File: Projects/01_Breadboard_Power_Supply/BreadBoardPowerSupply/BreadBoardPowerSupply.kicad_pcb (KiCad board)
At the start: 2 copper layers, 30.1 x 52.1 mm, 15 parts, among them J1 Barrel_Jack_Switch, J2 Conn_02x02_Odd_Even, J3 Conn_02x02_Odd_Even, SW1 SW_DPDT_x2, U1 LM7805_TO220

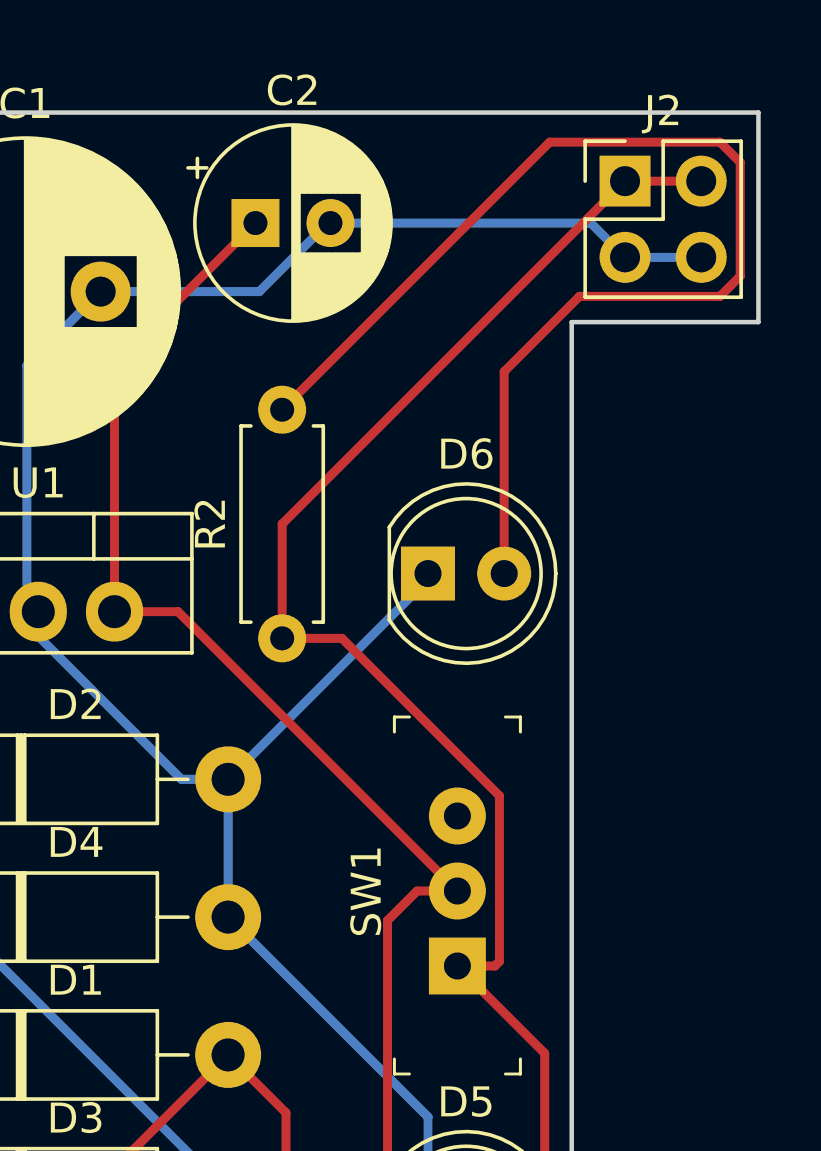
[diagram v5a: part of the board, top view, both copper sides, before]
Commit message: Rotate R2 to shorten wire length of F.Cu and finish routing
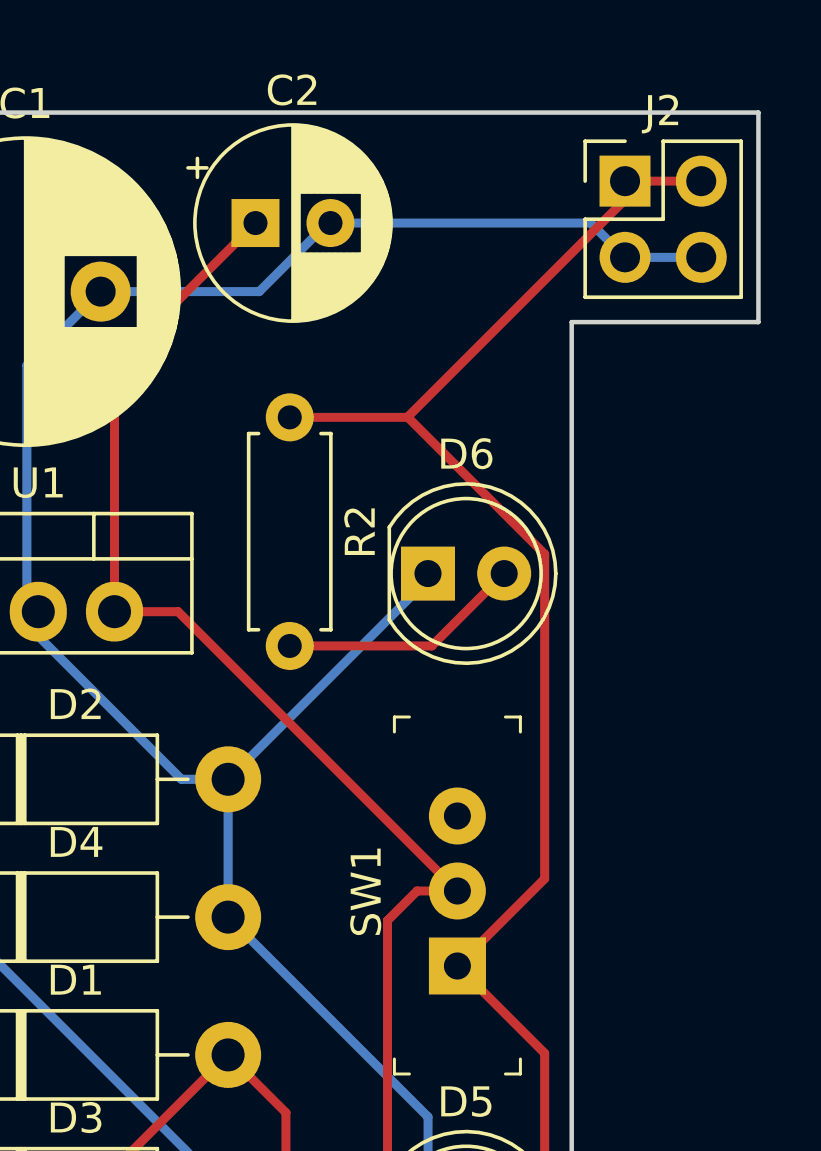
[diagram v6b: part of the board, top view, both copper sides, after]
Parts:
- moved R2 7.37 mm to (137.8, 82.7), turned to 270 degrees
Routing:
- net Net-(D6-Pad2): track 39.0 -> 8.15 mm
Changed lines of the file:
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@@
     (thickness 1.6)
     (drawings 8)
-    (tracks 74)
+    (tracks 68)
     (zones 0)
     (modules 15)
@@
     (add_net /Vout2)
     (add_net "Net-(D3-Pad2)")
+  )
+  (module Resistor_THT:R_Axial_DIN0207_L6.3mm_D2.5mm_P7.62mm_Horizontal (layer F.Cu)
+    (at 137.795 82.677 270)
+    (descr "Resistor, Axial_DIN0207 series, Axial, Horizontal, pin pitch=7.62mm, 0.25W = 1/4W, length*diameter=6.3*2.5mm^2, http://cdn-reichelt.de/documents/datenblatt/B400/1_4W%23YAG.pdf")
+    (tags "Resistor Axial_DIN0207 series Axial Horizontal pin pitch 7.62mm 0.25W = 1/4W length 6.3mm diameter 2.5mm")
+    (fp_text reference R2 (at 3.81 -2.37 90) (layer F.SilkS)
+      (effects (font (size 1 1) (thickness 0.15)))
+    )
+    (fp_text value "560 Ω" (at 3.81 2.37 90) (layer F.Fab)
+      (effects (font (size 1 1) (thickness 0.15)))
+    )
+    (fp_line (start 8.67 -1.5) (end -1.05 -1.5) (layer F.CrtYd) (width 0.05))
+    (fp_line (start 8.67 1.5) (end 8.67 -1.5) (layer F.CrtYd) (width 0.05))
+    (fp_line (start -1.05 1.5) (end 8.67 1.5) (layer F.CrtYd) (width 0.05))
+    (fp_line (start -1.05 -1.5) (end -1.05 1.5) (layer F.CrtYd) (width 0.05))
+    (fp_line (start 7.08 1.37) (end 7.08 1.04) (layer F.SilkS) (width 0.12))
+    (fp_line (start 0.54 1.37) (end 7.08 1.37) (layer F.SilkS) (width 0.12))
+    (fp_line (start 0.54 1.04) (end 0.54 1.37) (layer F.SilkS) (width 0.12))
+    (fp_line (start 7.08 -1.37) (end 7.08 -1.04) (layer F.SilkS) (width 0.12))
+    (fp_line (start 0.54 -1.37) (end 7.08 -1.37) (layer F.SilkS) (width 0.12))
+    (fp_line (start 0.54 -1.04) (end 0.54 -1.37) (layer F.SilkS) (width 0.12))
+    (fp_line (start 7.62 0) (end 6.96 0) (layer F.Fab) (width 0.1))
+    (fp_line (start 0 0) (end 0.66 0) (layer F.Fab) (width 0.1))
+    (fp_line (start 6.96 -1.25) (end 0.66 -1.25) (layer F.Fab) (width 0.1))
+    (fp_line (start 6.96 1.25) (end 6.96 -1.25) (layer F.Fab) (width 0.1))
+    (fp_line (start 0.66 1.25) (end 6.96 1.25) (layer F.Fab) (width 0.1))
+    (fp_line (start 0.66 -1.25) (end 0.66 1.25) (layer F.Fab) (width 0.1))
+    (fp_text user %R (at 3.81 0 90) (layer F.Fab)
+      (effects (font (size 1 1) (thickness 0.15)))
+    )
+    (pad 1 thru_hole circle (at 0 0 270) (size 1.6 1.6) (drill 0.8) (layers *.Cu *.Mask)
+      (net 9 /Vout2))
+    (pad 2 thru_hole oval (at 7.62 0 270) (size 1.6 1.6) (drill 0.8) (layers *.Cu *.Mask)
+      (net 7 "Net-(D6-Pad2)"))
+    (model ${KISYS3DMOD}/Resistor_THT.3dshapes/R_Axial_DIN0207_L6.3mm_D2.5mm_P7.62mm_Horizontal.wrl
+      (at (xyz 0 0 0))
+      (scale (xyz 1 1 1))
+      (rotate (xyz 0 0 0))
+    )
   )
   (module Capacitor_THT:CP_Radial_D10.0mm_P5.00mm (layer F.Cu)
@@
     )
   )
-  (module Resistor_THT:R_Axial_DIN0207_L6.3mm_D2.5mm_P7.62mm_Horizontal (layer F.Cu)
-    (at 137.541 90.043 90)
-    (descr "Resistor, Axial_DIN0207 series, Axial, Horizontal, pin pitch=7.62mm, 0.25W = 1/4W, length*diameter=6.3*2.5mm^2, http://cdn-reichelt.de/documents/datenblatt/B400/1_4W%23YAG.pdf")
-    (tags "Resistor Axial_DIN0207 series Axial Horizontal pin pitch 7.62mm 0.25W = 1/4W length 6.3mm diameter 2.5mm")
-    (fp_text reference R2 (at 3.81 -2.37 90) (layer F.SilkS)
-      (effects (font (size 1 1) (thickness 0.15)))
-    )
-    (fp_text value "560 Ω" (at 3.81 2.37 90) (layer F.Fab)
-      (effects (font (size 1 1) (thickness 0.15)))
-    )
-    (fp_line (start 8.67 -1.5) (end -1.05 -1.5) (layer F.CrtYd) (width 0.05))
-    (fp_line (start 8.67 1.5) (end 8.67 -1.5) (layer F.CrtYd) (width 0.05))
-    (fp_line (start -1.05 1.5) (end 8.67 1.5) (layer F.CrtYd) (width 0.05))
-    (fp_line (start -1.05 -1.5) (end -1.05 1.5) (layer F.CrtYd) (width 0.05))
-    (fp_line (start 7.08 1.37) (end 7.08 1.04) (layer F.SilkS) (width 0.12))
-    (fp_line (start 0.54 1.37) (end 7.08 1.37) (layer F.SilkS) (width 0.12))
-    (fp_line (start 0.54 1.04) (end 0.54 1.37) (layer F.SilkS) (width 0.12))
-    (fp_line (start 7.08 -1.37) (end 7.08 -1.04) (layer F.SilkS) (width 0.12))
-    (fp_line (start 0.54 -1.37) (end 7.08 -1.37) (layer F.SilkS) (width 0.12))
-    (fp_line (start 0.54 -1.04) (end 0.54 -1.37) (layer F.SilkS) (width 0.12))
-    (fp_line (start 7.62 0) (end 6.96 0) (layer F.Fab) (width 0.1))
-    (fp_line (start 0 0) (end 0.66 0) (layer F.Fab) (width 0.1))
-    (fp_line (start 6.96 -1.25) (end 0.66 -1.25) (layer F.Fab) (width 0.1))
-    (fp_line (start 6.96 1.25) (end 6.96 -1.25) (layer F.Fab) (width 0.1))
-    (fp_line (start 0.66 1.25) (end 6.96 1.25) (layer F.Fab) (width 0.1))
-    (fp_line (start 0.66 -1.25) (end 0.66 1.25) (layer F.Fab) (width 0.1))
-    (fp_text user %R (at 3.81 0 90) (layer F.Fab)
-      (effects (font (size 1 1) (thickness 0.15)))
-    )
-    (pad 1 thru_hole circle (at 0 0 90) (size 1.6 1.6) (drill 0.8) (layers *.Cu *.Mask)
-      (net 9 /Vout2))
-    (pad 2 thru_hole oval (at 7.62 0 90) (size 1.6 1.6) (drill 0.8) (layers *.Cu *.Mask)
-      (net 7 "Net-(D6-Pad2)"))
-    (model ${KISYS3DMOD}/Resistor_THT.3dshapes/R_Axial_DIN0207_L6.3mm_D2.5mm_P7.62mm_Horizontal.wrl
-      (at (xyz 0 0 0))
-      (scale (xyz 1 1 1))
-      (rotate (xyz 0 0 0))
-    )
-  )
   (module digikey-footprints:Switch_Slide_11.6x4mm_EG1218 locked (layer F.Cu)
     (at 143.383 100.965 90)
@@
   (segment (start 145.014001 109.545001) (end 144.943 109.474) (width 0.3) (layer F.Cu) (net 6))
   (segment (start 143.764 122.809) (end 145.014001 121.558999) (width 0.3) (layer F.Cu) (net 6))
-  (segment (start 144.943 81.150946) (end 144.943 87.884) (width 0.3) (layer F.Cu) (net 7))
-  (segment (start 147.450945 78.643001) (end 144.943 81.150946) (width 0.3) (layer F.Cu) (net 7))
-  (segment (start 152.135001 78.643001) (end 147.450945 78.643001) (width 0.3) (layer F.Cu) (net 7))
-  (segment (start 152.811001 77.967001) (end 152.135001 78.643001) (width 0.3) (layer F.Cu) (net 7))
-  (segment (start 152.811001 74.178999) (end 152.811001 77.967001) (width 0.3) (layer F.Cu) (net 7))
-  (segment (start 152.135001 73.502999) (end 152.811001 74.178999) (width 0.3) (layer F.Cu) (net 7))
-  (segment (start 146.461001 73.502999) (end 152.135001 73.502999) (width 0.3) (layer F.Cu) (net 7))
-  (segment (start 137.541 82.423) (end 146.461001 73.502999) (width 0.3) (layer F.Cu) (net 7))
+  (segment (start 142.53 90.297) (end 144.943 87.884) (width 0.3) (layer F.Cu) (net 7))
+  (segment (start 137.795 90.297) (end 142.53 90.297) (width 0.3) (layer F.Cu) (net 7))
   (segment (start 151.511 119.761) (end 148.971 119.761) (width 0.3) (layer F.Cu) (net 9))
   (segment (start 146.293001 103.875001) (end 143.383 100.965) (width 0.3) (layer F.Cu) (net 9))
@@
   (segment (start 148.609524 119.761) (end 146.293001 117.444477) (width 0.3) (layer F.Cu) (net 9))
   (segment (start 148.971 119.761) (end 148.609524 119.761) (width 0.3) (layer F.Cu) (net 9))
-  (segment (start 144.783001 95.292999) (end 139.533002 90.043) (width 0.3) (layer F.Cu) (net 9))
-  (segment (start 144.783001 100.814999) (end 144.783001 95.292999) (width 0.3) (layer F.Cu) (net 9))
-  (segment (start 139.533002 90.043) (end 137.541 90.043) (width 0.3) (layer F.Cu) (net 9))
-  (segment (start 144.633 100.965) (end 144.783001 100.814999) (width 0.3) (layer F.Cu) (net 9))
-  (segment (start 143.383 100.965) (end 144.633 100.965) (width 0.3) (layer F.Cu) (net 9))
   (segment (start 148.971 74.803) (end 151.511 74.803) (width 0.3) (layer F.Cu) (net 9))
-  (segment (start 137.541 86.233) (end 137.541 90.043) (width 0.3) (layer F.Cu) (net 9))
-  (segment (start 148.971 74.803) (end 137.541 86.233) (width 0.3) (layer F.Cu) (net 9))
+  (segment (start 141.734002 82.677) (end 137.795 82.677) (width 0.3) (layer F.Cu) (net 9))
+  (segment (start 146.293001 87.235999) (end 141.734002 82.677) (width 0.3) (layer F.Cu) (net 9))
+  (segment (start 146.293001 98.054999) (end 146.293001 87.235999) (width 0.3) (layer F.Cu) (net 9))
+  (segment (start 143.383 100.965) (end 146.293001 98.054999) (width 0.3) (layer F.Cu) (net 9))
+  (segment (start 148.971 75.418998) (end 148.971 74.803) (width 0.3) (layer F.Cu) (net 9))
+  (segment (start 141.734002 82.655996) (end 148.971 75.418998) (width 0.3) (layer F.Cu) (net 9))
+  (segment (start 141.734002 82.677) (end 141.734002 82.655996) (width 0.3) (layer F.Cu) (net 9))
 )

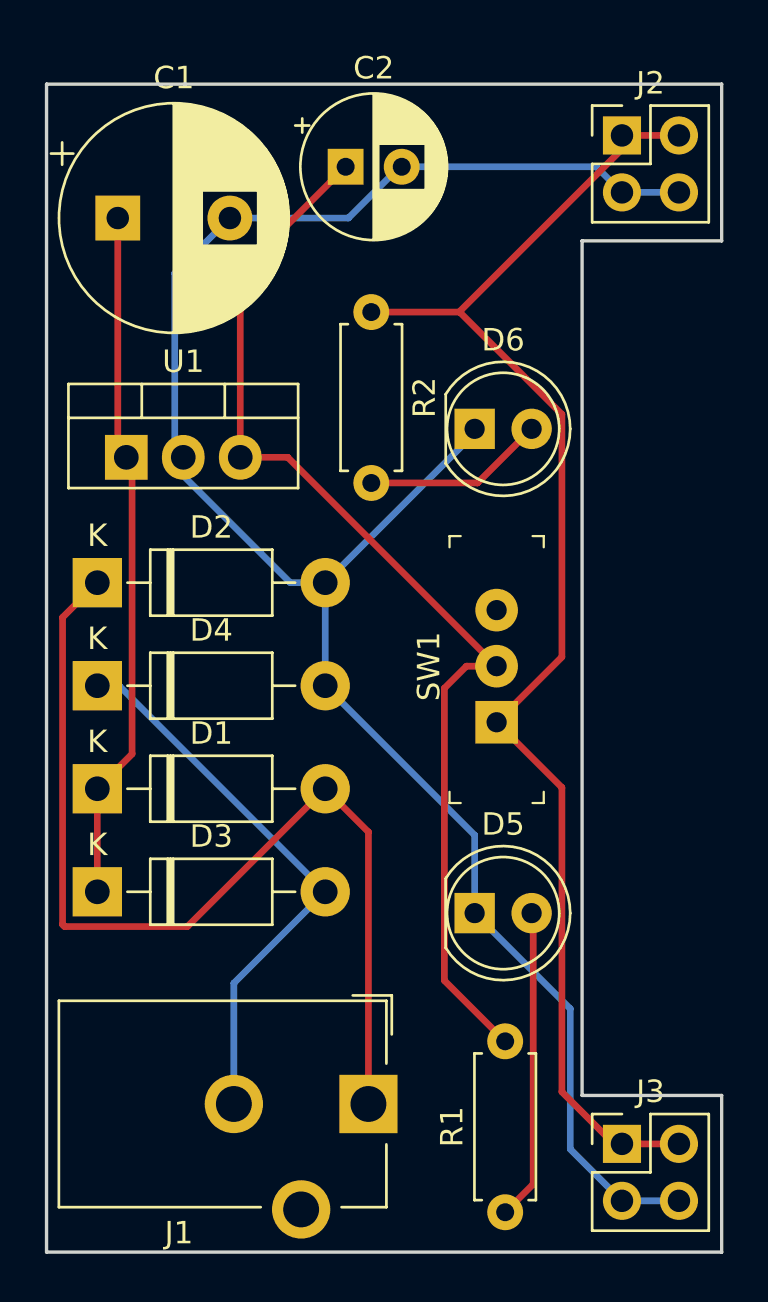
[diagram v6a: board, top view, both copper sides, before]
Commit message: Add copper fill on B.Cu and run DRC: 	- V- only 	- Add thermal reliefs
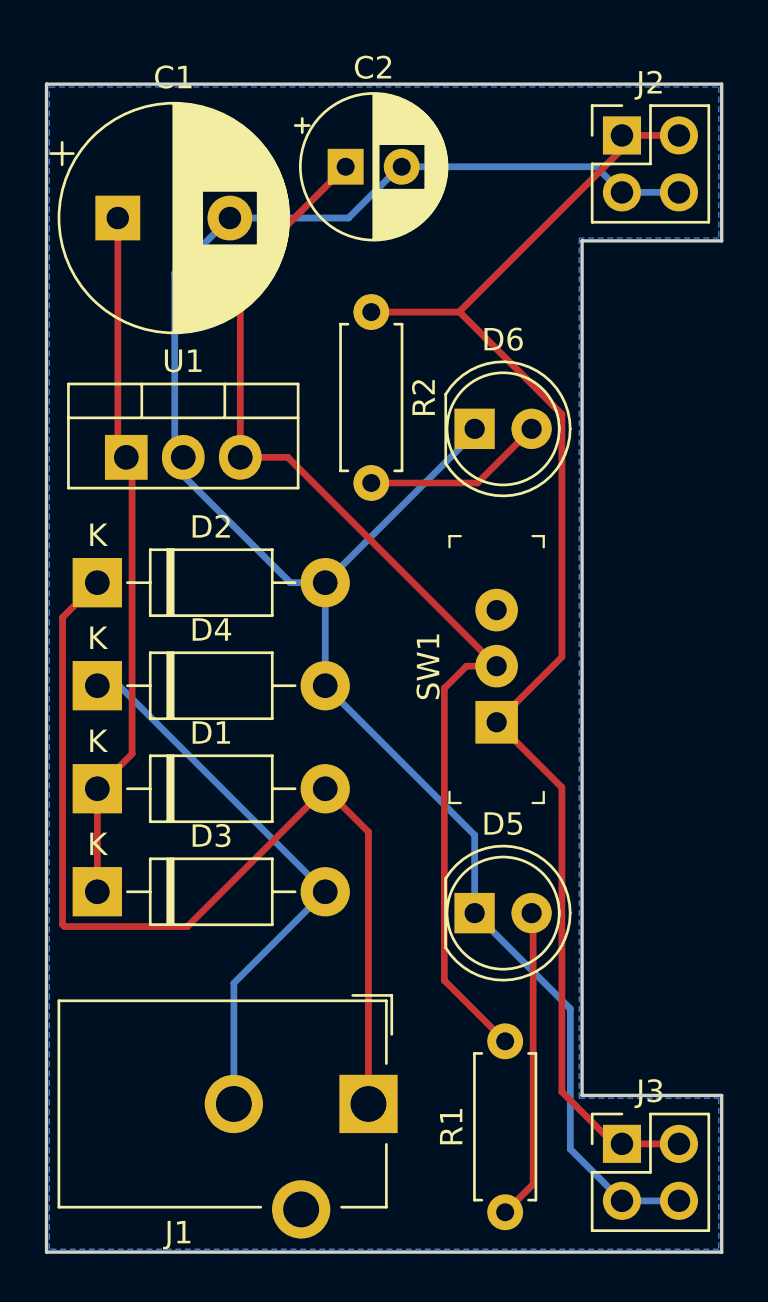
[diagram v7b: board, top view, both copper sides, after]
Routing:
- added copper zone on B.Cu, net /V-

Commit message: Add silkscreen text and graphics: 	- Describe pads 	- Board version 	- Logos 	- Other Instructions 	- Added a PNG image of the 3=D PCB 	- Fixed Eeschema capacitors - C1 and C2 needed to their values 	  swapped
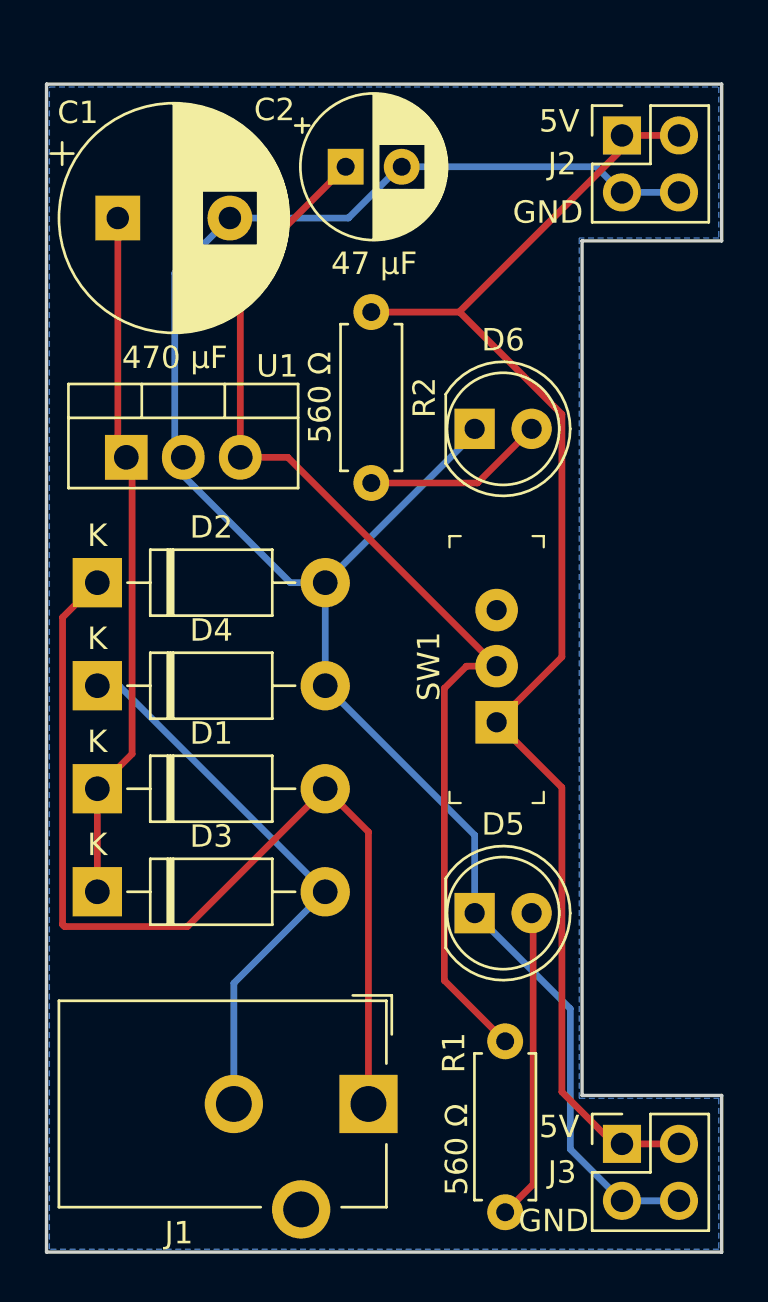
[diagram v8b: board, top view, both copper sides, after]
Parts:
- added REF**: OSHW-Logo2_7.3x6mm_SilkScreen, Symbol:OSHW-Logo2_7.3x6mm_SilkScreen, B.Cu at (137.8, 86.4)
- added REF**: KiCad-Logo2_8mm_SilkScreen, Symbol:KiCad-Logo2_8mm_SilkScreen, B.Cu at (135.3, 78.7)
- C1: value 47 μF -> 470 μF
- C2: value 470 μF -> 47 μF
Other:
- board text added: "47 μF"
- board text added: "470 μF"
- board text added: "560 Ω"
- board text added: "5V"
- board text added: "Breadboard Power Supply V1.0"
- board text added: "GND"
- board text added: "github.com/Michael-Q-Ly"
